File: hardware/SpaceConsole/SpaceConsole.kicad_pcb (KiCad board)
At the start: 2 copper layers, 80 x 55.9 mm, 18 parts, among them IC1 ArduinoProMini, J1 LeftFrontLED, J2 RightFrontLED, J3 LeftMiddleLED, J4 RightMiddleLED, J5 RearLED, J6 SwitchA, J7 Battery, J9 Power_Switch, SW1 KnobB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

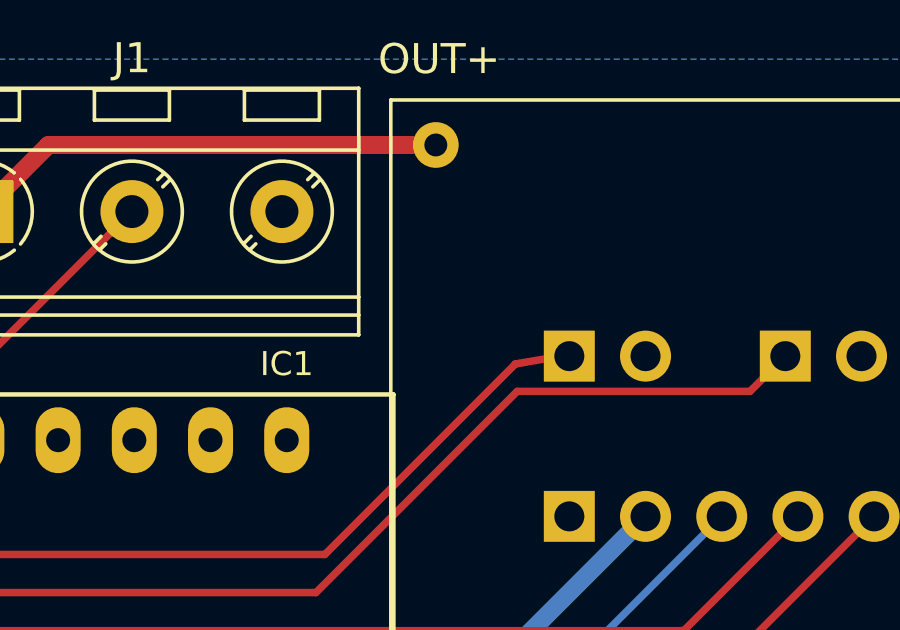
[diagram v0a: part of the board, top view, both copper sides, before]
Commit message: Update silk screen
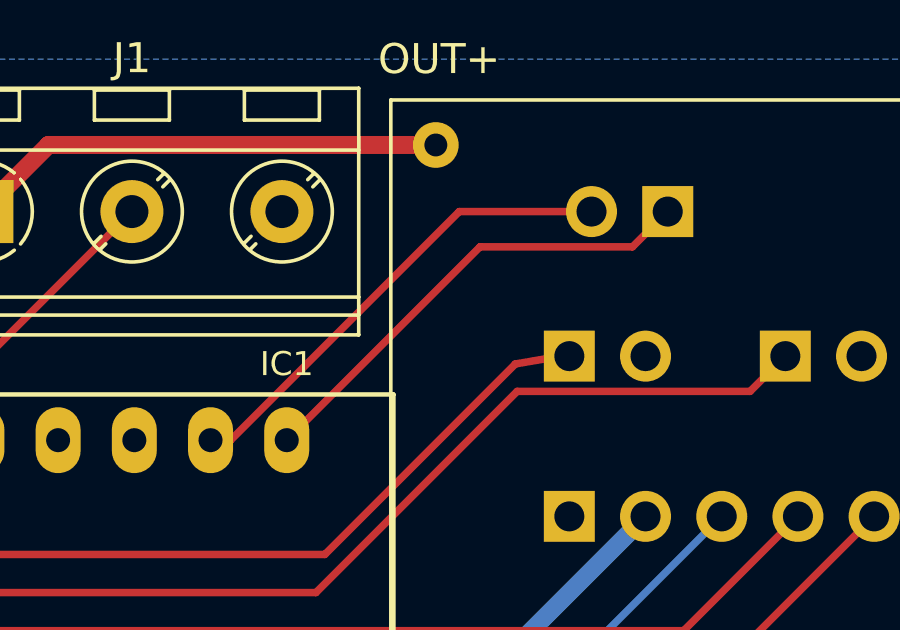
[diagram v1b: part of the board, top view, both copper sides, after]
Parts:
- added J8: Serial_Port, Connector_PinHeader_2.54mm:PinHeader_1x02_P2.54mm_Vertical, B.Cu at (190.5, 83.8)
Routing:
- net Net-(IC1-Pad2): track 0.00 -> 15.9 mm
- net Net-(IC1-Pad1): track 0.00 -> 15.9 mm
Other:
- board text added: "RX"
- board text added: "TX"
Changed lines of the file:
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@@
   (general
     (thickness 1.6)
-    (drawings 4)
-    (tracks 95)
+    (drawings 8)
+    (tracks 101)
     (zones 0)
-    (modules 18)
+    (modules 19)
     (nets 32)
   )
@@
     (46 B.CrtYd user)
     (47 F.CrtYd user)
-    (48 B.Fab user)
-    (49 F.Fab user)
+    (48 B.Fab user hide)
+    (49 F.Fab user hide)
   )
   (setup
@@
     (pad_to_mask_clearance 0)
     (aux_axis_origin 0 0)
-    (visible_elements FFFFFF7F)
+    (visible_elements FFFFEF7F)
     (pcbplotparams
       (layerselection 0x010fc_ffffffff)
@@
     (add_net VCC)
   )
+  (module Connector_PinHeader_2.54mm:PinHeader_1x02_P2.54mm_Vertical (layer B.Cu)
+    (at 190.5 83.82 90)
+    (descr "Through hole straight pin header, 1x02, 2.54mm pitch, single row")
+    (tags "Through hole pin header THT 1x02 2.54mm single row")
+    (fp_text reference J8 (at 0 2.33) (layer B.SilkS)
+      (effects (font (size 1 1) (thickness 0.15)) (justify mirror))
+    )
+    (fp_text value Serial_Port (at 0 -4.87 -90) (layer B.Fab)
+      (effects (font (size 1 1) (thickness 0.15)) (justify mirror))
+    )
+    (fp_text user %R (at 0 -1.27) (layer B.Fab)
+      (effects (font (size 1 1) (thickness 0.15)) (justify mirror))
+    )
+    (fp_line (start -0.635 1.27) (end 1.27 1.27) (layer B.Fab) (width 0.1))
+    (fp_line (start 1.27 1.27) (end 1.27 -3.81) (layer B.Fab) (width 0.1))
+    (fp_line (start 1.27 -3.81) (end -1.27 -3.81) (layer B.Fab) (width 0.1))
+    (fp_line (start -1.27 -3.81) (end -1.27 0.635) (layer B.Fab) (width 0.1))
+    (fp_line (start -1.27 0.635) (end -0.635 1.27) (layer B.Fab) (width 0.1))
+    (fp_line (start -1.33 -3.87) (end 1.33 -3.87) (layer B.SilkS) (width 0.12))
+    (fp_line (start -1.33 -1.27) (end -1.33 -3.87) (layer B.SilkS) (width 0.12))
+    (fp_line (start 1.33 -1.27) (end 1.33 -3.87) (layer B.SilkS) (width 0.12))
+    (fp_line (start -1.33 -1.27) (end 1.33 -1.27) (layer B.SilkS) (width 0.12))
+    (fp_line (start -1.33 0) (end -1.33 1.33) (layer B.SilkS) (width 0.12))
+    (fp_line (start -1.33 1.33) (end 0 1.33) (layer B.SilkS) (width 0.12))
+    (fp_line (start -1.8 1.8) (end -1.8 -4.35) (layer B.CrtYd) (width 0.05))
+    (fp_line (start -1.8 -4.35) (end 1.8 -4.35) (layer B.CrtYd) (width 0.05))
+    (fp_line (start 1.8 -4.35) (end 1.8 1.8) (layer B.CrtYd) (width 0.05))
+    (fp_line (start 1.8 1.8) (end -1.8 1.8) (layer B.CrtYd) (width 0.05))
+    (pad 2 thru_hole oval (at 0 -2.54 90) (size 1.7 1.7) (drill 1) (layers *.Cu *.Mask)
+      (net 24 "Net-(IC1-Pad2)"))
+    (pad 1 thru_hole rect (at 0 0 90) (size 1.7 1.7) (drill 1) (layers *.Cu *.Mask)
+      (net 25 "Net-(IC1-Pad1)"))
+    (model ${KISYS3DMOD}/Connector_PinHeader_2.54mm.3dshapes/PinHeader_1x02_P2.54mm_Vertical.wrl
+      (at (xyz 0 0 0))
+      (scale (xyz 1 1 1))
+      (rotate (xyz 0 0 0))
+    )
+  )
   (module MountingHole:MountingHole_3.2mm_M3 (layer F.Cu)
     (at 205.74 125.73)
@@
     (descr "Through hole straight pin header, 1x02, 2.54mm pitch, single row")
     (tags "Through hole pin header THT 1x02 2.54mm single row")
-    (fp_text reference SW4 (at 0 2.33 270) (layer B.SilkS)
+    (fp_text reference SW4 (at 0.261569 -6.24) (layer B.SilkS)
       (effects (font (size 1 1) (thickness 0.15)) (justify mirror))
     )
@@
     (descr "Through hole straight pin header, 1x02, 2.54mm pitch, single row")
     (tags "Through hole pin header THT 1x02 2.54mm single row")
-    (fp_text reference SW3 (at 0 2.33 270) (layer B.SilkS)
+    (fp_text reference SW3 (at 0.261569 3.07) (layer B.SilkS)
       (effects (font (size 1 1) (thickness 0.15)) (justify mirror))
     )
@@
     (descr "Through hole straight pin header, 1x05, 2.54mm pitch, single row")
     (tags "Through hole pin header THT 1x05 2.54mm single row")
-    (fp_text reference SW2 (at 0 2.33 270) (layer B.SilkS)
+    (fp_text reference SW2 (at 0 3.07) (layer B.SilkS)
       (effects (font (size 1 1) (thickness 0.15)) (justify mirror))
     )
@@
     (descr "Through hole straight pin header, 1x05, 2.54mm pitch, single row")
     (tags "Through hole pin header THT 1x05 2.54mm single row")
-    (fp_text reference SW1 (at 0 2.33 270) (layer B.SilkS)
+    (fp_text reference SW1 (at -0.178431 3.07) (layer B.SilkS)
       (effects (font (size 1 1) (thickness 0.15)) (justify mirror))
     )
@@
     (descr "Buzzer, D12.2mm height 6.5mm, https://product.tdk.com/info/en/catalog/datasheets/piezoelectronic_buzzer_ps_en.pdf")
     (tags buzzer)
-    (fp_text reference BZ1 (at 2.5 7.17 270) (layer B.SilkS)
+    (fp_text reference BZ1 (at 2.5 -8.89) (layer B.SilkS)
       (effects (font (size 1 1) (thickness 0.15)) (justify mirror))
     )
@@
     (descr "Through hole straight pin header, 1x02, 2.54mm pitch, single row")
     (tags "Through hole pin header THT 1x02 2.54mm single row")
-    (fp_text reference J9 (at 0 2.33 270) (layer B.SilkS)
+    (fp_text reference J9 (at 0 2.54) (layer B.SilkS)
       (effects (font (size 1 1) (thickness 0.15)) (justify mirror))
     )
@@
       (rotate (xyz 0 0 0))
     )
+  )
+  (gr_circle (center 186.1 109.87) (end 186.05 109.85) (layer B.SilkS) (width 0.12))
+  (gr_circle (center 185.57 91.86) (end 185.5 91.83) (layer B.SilkS) (width 0.12))
+  (gr_text TX (at 190.5 81.28) (layer B.SilkS)
+    (effects (font (size 1 1) (thickness 0.25)) (justify mirror))
+  )
+  (gr_text RX (at 187.96 81.28) (layer B.SilkS)
+    (effects (font (size 1 1) (thickness 0.25)) (justify mirror))
   )
   (gr_line (start 129.54 129.54) (end 129.54 73.66) (layer Edge.Cuts) (width 0.05))
@@
   (segment (start 167.64 88.82) (end 172.64 83.82) (width 0.25) (layer F.Cu) (net 21))
   (segment (start 167.64 91.44) (end 167.64 88.82) (width 0.25) (layer F.Cu) (net 21))
+  (segment (start 175.929651 91.44) (end 175.26 91.44) (width 0.25) (layer F.Cu) (net 24))
+  (segment (start 183.549651 83.82) (end 175.929651 91.44) (width 0.25) (layer F.Cu) (net 24))
+  (segment (start 187.96 83.82) (end 183.549651 83.82) (width 0.25) (layer F.Cu) (net 24))
+  (segment (start 189.324999 84.995001) (end 184.244999 84.995001) (width 0.25) (layer F.Cu) (net 25))
+  (segment (start 184.244999 84.995001) (end 177.8 91.44) (width 0.25) (layer F.Cu) (net 25))
+  (segment (start 190.5 83.82) (end 189.324999 84.995001) (width 0.25) (layer F.Cu) (net 25))
   (segment (start 199.507999 122.862001) (end 200.77 121.6) (width 0.6) (layer F.Cu) (net 26))
   (segment (start 173.742001 122.862001) (end 199.507999 122.862001) (width 0.6) (layer F.Cu) (net 26))
